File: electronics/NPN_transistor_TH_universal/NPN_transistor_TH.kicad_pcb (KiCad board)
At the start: 2 copper layers, 19 x 19 mm, 7 parts, among them J1 B, J2 E, J3 C, J4 E, Q1 BC547

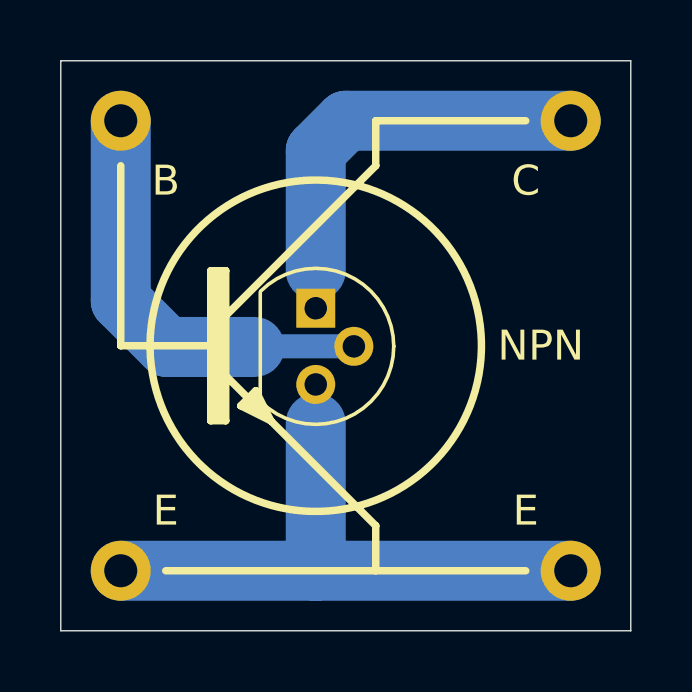
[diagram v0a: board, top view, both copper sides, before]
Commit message: added universal NPN transistor board
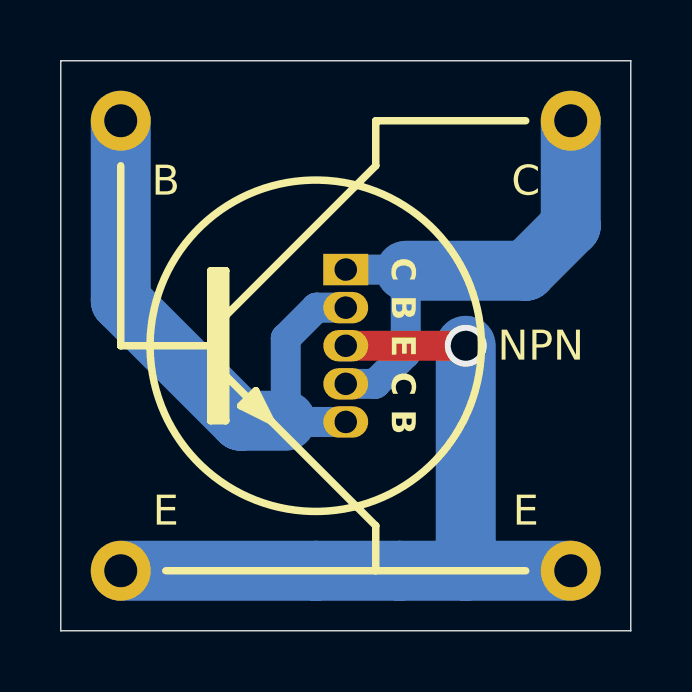
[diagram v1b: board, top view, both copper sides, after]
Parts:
- N1: value V20201122 -> V20240522
- Q1: footprint Package_TO_SOT_THT:TO-92 -> SquantorIC:TO-92L_Inline_transistor_CBEBC
- moved Q1 1.60 mm to (149.5, 70.5)
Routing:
- net Net-(J1-Pin_1): track 14.4 -> 20.3 mm
- net Net-(J2-Pin_1): track 21.2 -> 26.5 mm, vias 0 -> 1
- net Net-(J3-Pin_1): track 14.2 -> 16.8 mm
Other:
- rule pad_to_mask_clearance: 0.0762 -> 0
